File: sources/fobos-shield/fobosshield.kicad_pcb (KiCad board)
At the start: 2 copper layers, 83.8 x 63.5 mm, 156 parts, among them J1 Target, J10 ADCin, J11 PP1, J12 PP2, J13 Clock, J14 Trigger, J15 CSM5VCur, J16 Conn_01x01, J17 Barrel_Jack_Switch, J18 Conn_01x02, J19 Conn_01x02, J2 Glitch, J20 CSM3V3Cur, J21 GND, J22 GND, J3 Analog, J4 IOH, J5 SPI, J6 Analog2, J7 Power, J8 IOL, J9 SPI2, Q1 IRF7807Z, Q2 IRLML2502, Q3 BSS123, Q4 BSS84, U1 NMA0509SC, U10 INA225, U11 INA225, U12 LD1117S33TR_SOT223, U2 NMA0509SC, U3 LM317L_SO8, U4 LM337L_SO8, U5 LD59015, U6 LD3985G33R_TSOT23, U7 AD8331, U8 TPS7A7100_VQFN16, U9 AD9215

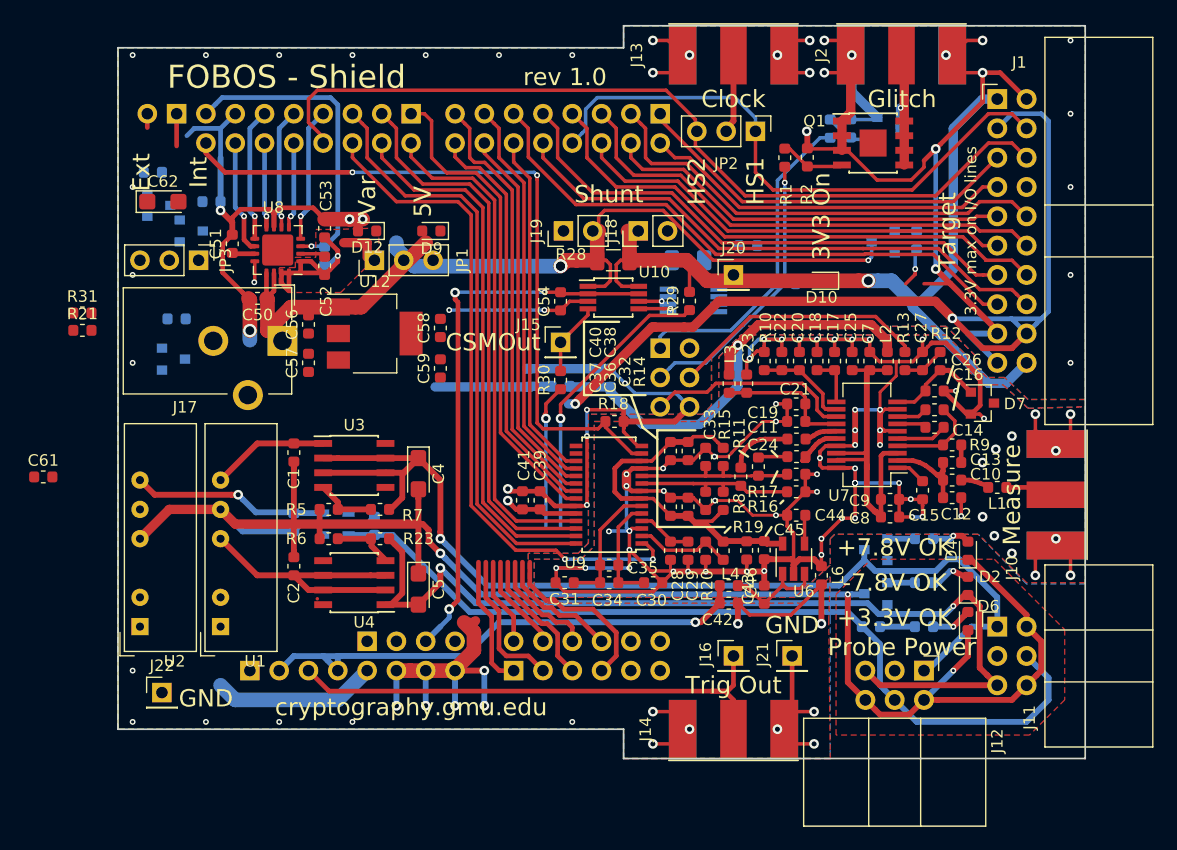
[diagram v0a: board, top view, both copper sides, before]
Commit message: variable power new layout
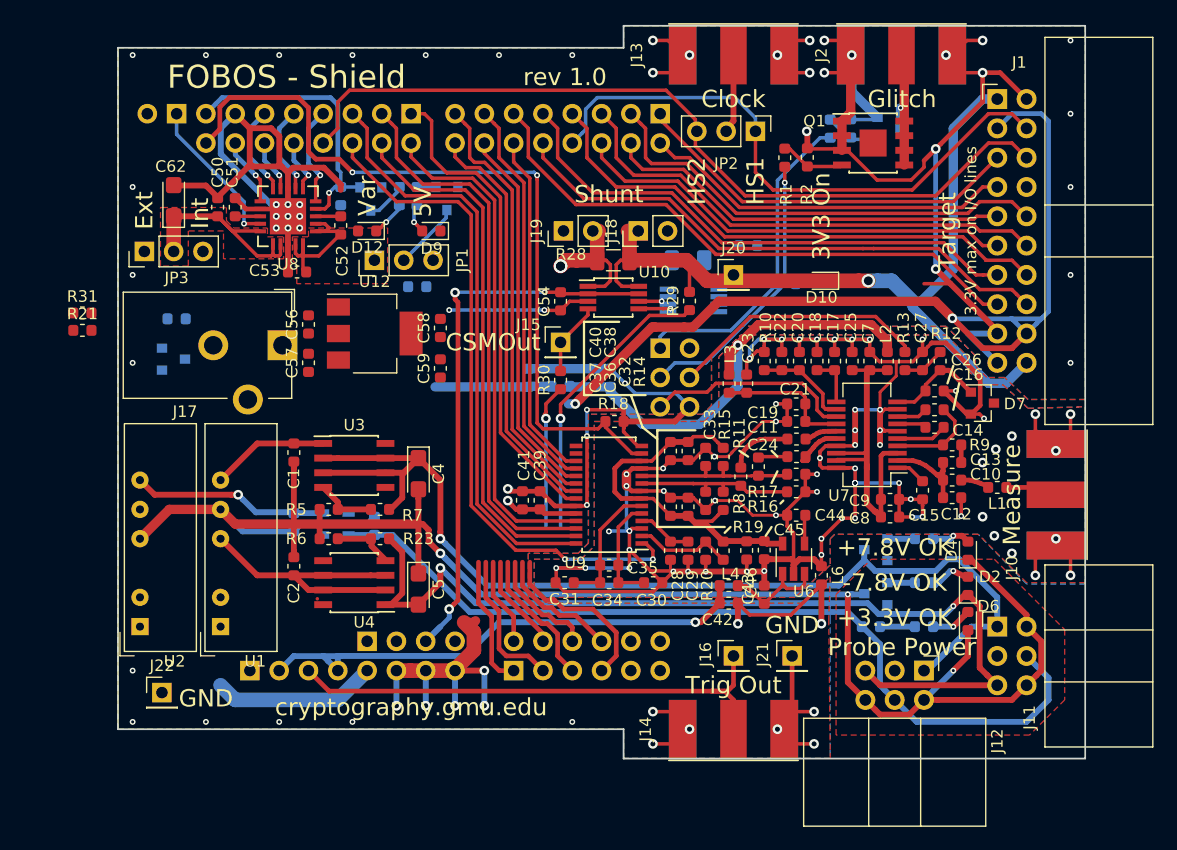
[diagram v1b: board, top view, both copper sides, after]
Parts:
- removed Q4: BSS84, Package_TO_SOT_SMD:SOT-23
- removed R34: 10K, Resistor_SMD:R_0603_1608Metric
- C61: moved to B.Cu
- U8: value TPS7A7100_VQFN16 -> TPS7A7100_VQFN20; footprint cerg:Texas_S-PVQFN-N16_EP2.7x2.7mm -> Package_DFN_QFN:Texas_VQFN-RGW-20
- moved R27 43.5 mm to (62.7, 37.6)
- moved D8 38.0 mm to (65.3, 37.8), turned to 270 degrees
- moved C61 36.4 mm to (62.8, 45.5), turned to 180 degrees
- moved Q3 18.4 mm to (58.7, 37.9), turned to 270 degrees
- moved R35 16.3 mm to (61.2, 37.6), turned to 270 degrees
- moved C50 8.62 mm to (45.5, 38.6), turned to 90 degrees
- moved R22 5.37 mm to (56.1, 37.6), turned to 90 degrees
- moved JP3 4.76 mm to (39.1, 42.4), turned to 90 degrees
- moved C53 4.47 mm to (52.3, 44.2), turned to 180 degrees
- moved C52 3.77 mm to (56.1, 40.2)
- moved C51 3.19 mm to (47.0, 38.6)
- moved U8 3.05 mm to (51.6, 39.4)
- moved C62 0.94 mm to (41.7, 38.0), turned to 90 degrees
- moved J17 0.38 mm to (51.1, 50.5)
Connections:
- C50 pad 1: VCC -> IN
- C56 pad 1: VCC -> IN
- C57 pad 1: VCC -> IN
- C60 pad 1: VCC -> IN
- C61 pad 1: VCC -> IN
- C62 pad 1: VCC -> IN
- D12 pad 1: GND -> Net-(D12-Pad1)
- D12 pad 2: Net-(D12-Pad2) -> VCC3V3
- JP1 pad 3: VCC -> IN
- JP3 pad 2: VCC -> IN
- R35 pad 1: Net-(Q4-Pad3) -> Net-(Q3-Pad3)
- R35 pad 2: Net-(D12-Pad2) -> Net-(D12-Pad1)
- U1 pad 1: VCC -> IN
- U12 pad 3: VCC -> IN
- U2 pad 1: VCC -> IN
- U8 pad 10: PWR5 -> PWR4
- U8 pad 11: Net-(C51-Pad1) -> PWR5
- U8 pad 12: PWR_EN -> GND
- U8 pad 13: VCC -> Net-(C51-Pad1)
- U8 pad 14: VCC -> PWR_EN
- U8 pad 15: Net-(C52-Pad1) -> IN
- U8 pad 16: Net-(C52-Pad1) -> IN
- U8 pad 17: (no net) -> IN
- U8 pad 2: Net-(C52-Pad2) -> Net-(C52-Pad1)
- U8 pad 3: PWR_PG -> Net-(C52-Pad2)
- U8 pad 4: PWR0 -> PWR_PG
- U8 pad 5: PWR1 -> PWR0
- U8 pad 6: PWR2 -> PWR1
- U8 pad 7: GND -> PWR2
- U8 pad 8: PWR3 -> GND
- U8 pad 9: PWR4 -> PWR3
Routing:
- net Net-(D8-Pad1): track 54.5 -> 16.7 mm, vias 3 -> 2
- net VCC5V0: track 61.5 -> 36.7 mm
- net IN: track 0.00 -> 20.2 mm
- net PWR_EN: track 4.63 -> 13.3 mm
- net GND: track 250.4 -> 258.7 mm, vias 58 -> 63
- net ADC_CLK: track 63.5 -> 69.6 mm
- net Net-(C52-Pad1): track 19.7 -> 13.9 mm, vias 1 -> 0
- net PWR5: track 9.86 -> 5.95 mm
- net PWR4: track 11.5 -> 7.85 mm
- net Net-(Q3-Pad3): track 0.00 -> 3.47 mm
- net Net-(D12-Pad1): track 0.00 -> 3.02 mm, vias 0 -> 1
- net PWR0: track 11.6 -> 8.70 mm
- net PWR1: track 7.52 -> 4.67 mm
- net PWR3: track 7.86 -> 5.03 mm
- net PWR2: track 10.9 -> 8.20 mm
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- added copper zone on F.Cu, net IN

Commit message: 3V3 CSM layouted
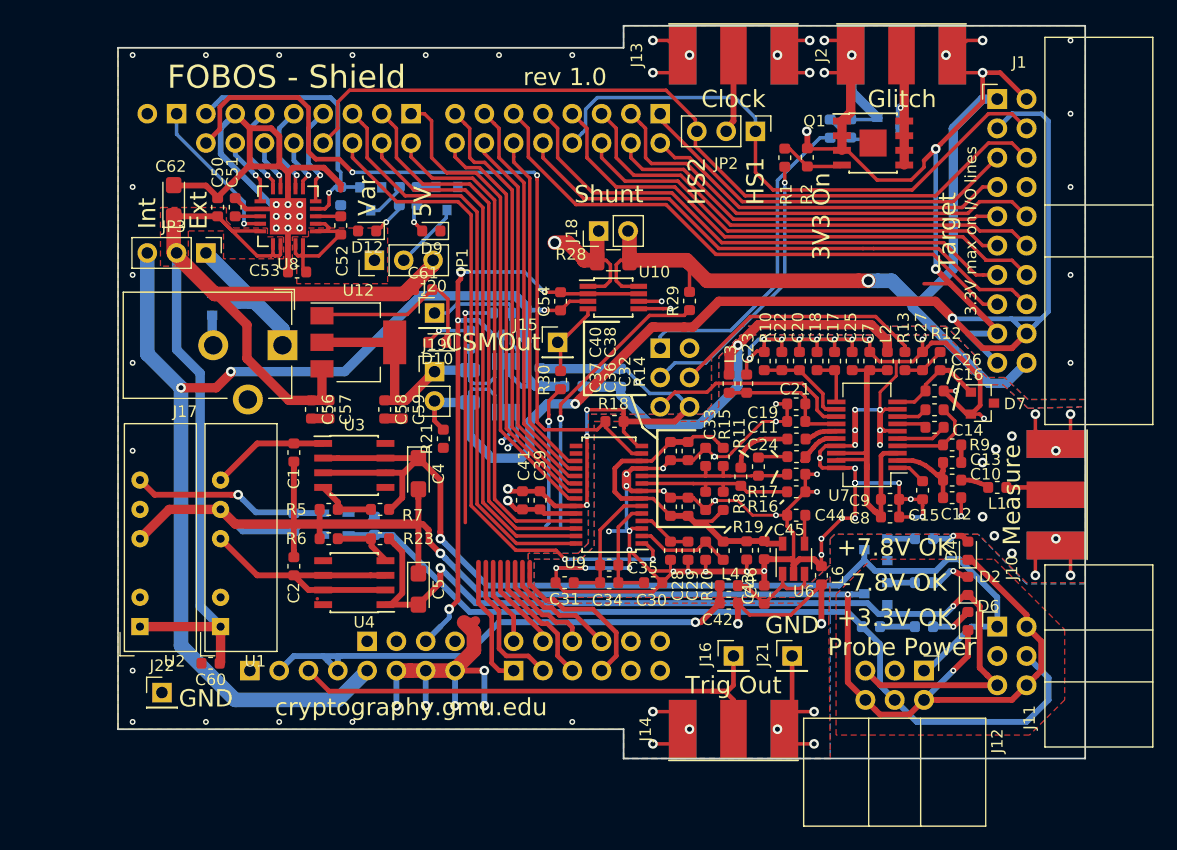
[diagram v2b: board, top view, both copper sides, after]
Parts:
- C60, C61: moved to F.Cu
- R31: moved to B.Cu
- moved R31 36.4 mm to (70.1, 47.8)
- moved D10 33.7 mm to (64.5, 50.3)
- moved R21 32.7 mm to (65.0, 58.6), turned to 90 degrees
- moved C60 30.0 mm to (44.9, 78.1), turned to 180 degrees
- moved R33 27.9 mm to (67.3, 50.1), turned to 90 degrees
- moved J20 26.1 mm to (64.3, 47.8)
- moved C55 21.9 mm to (71.0, 49.7), turned to 180 degrees
- moved R32 21.8 mm to (67.3, 54.1), turned to 270 degrees
- moved U11 17.9 mm to (70.4, 54.1), turned to 270 degrees
- moved J19 16.5 mm to (64.3, 52.8), turned to 0 degrees
- moved C58 8.55 mm to (59.9, 56.1), turned to 270 degrees
- moved C56 7.37 mm to (53.6, 56.1), turned to 270 degrees
- moved D11 6.45 mm to (46.0, 47.0)
- moved JP3 5.34 mm to (44.5, 42.5), turned to 270 degrees
- moved C59 4.85 mm to (61.5, 56.1), turned to 270 degrees
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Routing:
- net IN: track 20.2 -> 112.9 mm
- net VCC5V0: track 36.7 -> 108.3 mm, vias 2 -> 3
- net Net-(C58-Pad1): track 0.00 -> 26.3 mm
- net CSM3V3: track 79.9 -> 106.3 mm
- net GND: track 258.7 -> 279.4 mm, vias 63 -> 64
- net /Ardu/A3: track 15.0 -> 35.5 mm, vias 0 -> 1
- net XADCGND: track 47.5 -> 60.6 mm, vias 3 -> 4
- net Net-(D11-Pad1): track 0.00 -> 12.7 mm
- net CSM3V3Cur: track 0.00 -> 12.0 mm
- net Net-(D10-Pad2): track 0.00 -> 4.07 mm, vias 0 -> 1
- net CSM3V3Gain0: track 9.80 -> 13.2 mm, vias 0 -> 1
- net CSM3V3Gain1: track 10.9 -> 13.8 mm, vias 0 -> 1
- net 5Vclean: track 39.3 -> 38.2 mm
- net Net-(D8-Pad1): track 16.7 -> 17.7 mm, vias 2 -> 1

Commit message: all routed, needs DRC
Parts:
- added G***: LOGO, cerg:cerg, F.Cu at (97.0, 41.7)
- moved R29 1.65 mm to (84.7, 46.7)
- moved J15 0.76 mm to (75.7, 50.3)
- moved J19 0.13 mm to (64.1, 52.8)
- moved J20 0.13 mm to (64.1, 47.8)
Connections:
- J3 pad 2: CSM5VGain0 -> CSM3V3Gain1
- J3 pad 4: CSM5VGain1 -> CSM3V3Gain0
- J3 pad 6: CSM3V3Gain0 -> CSM5VGain1
- J3 pad 8: CSM3V3Gain1 -> CSM5VGain0
- R21 pad 1: /Ardu/A2 -> /Ardu/A0
- R29 pad 1: /Ardu/A0 -> /Ardu/A3
- R30 pad 1: /Ardu/A1 -> /Ardu/A2
- R31 pad 1: /Ardu/A3 -> /Ardu/A1
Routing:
- net GND: track 279.4 -> 473.8 mm, vias 64 -> 86
- net VCC3V3: track 51.9 -> 103.2 mm, vias 2 -> 6
- net CSM5VGain0: track 10.4 -> 38.4 mm, vias 1 -> 2
- net CSM5VGain1: track 10.4 -> 37.8 mm, vias 1 -> 2
- net /Ardu/A2: track 12.0 -> 29.3 mm, vias 0 -> 2
- net Net-(D8-Pad1): track 17.7 -> 32.1 mm
- net /Ardu/A0: track 36.6 -> 22.6 mm, vias 1 -> 2
- net /Ardu/A1: track 24.9 -> 37.5 mm
- net CSM3V3Gain0: track 13.2 -> 23.8 mm, vias 1 -> 3
- net CSM3V3Gain1: track 13.8 -> 22.8 mm, vias 1 -> 3
- net /Ardu/A3: track 35.5 -> 44.2 mm, vias 1 -> 2
- net Net-(D11-Pad1): track 12.7 -> 17.1 mm
- net Net-(C52-Pad1): track 13.9 -> 17.8 mm
- net Net-(C3-Pad1): track 17.0 -> 20.3 mm
- net /Power/GNDP: track 147.5 -> 150.2 mm
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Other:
- board text added: "3V3"
- board text added: "CSM"
- board text added: "CSM 5V/Var"
- board text added: "Out"
- board text added: "Shnt"
- board text removed: "3V3 On"
- board text removed: "CSMOut"
- board text removed: "Shunt"

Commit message: DRC passes
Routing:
- net GNDA: track 228.2 -> 230.5 mm, vias 65 -> 66
- net IN: track 112.9 -> 111.2 mm
- net 5Vclean: track 37.9 -> 36.6 mm
- net GND: track 473.8 -> 473.6 mm, vias 86 -> 89

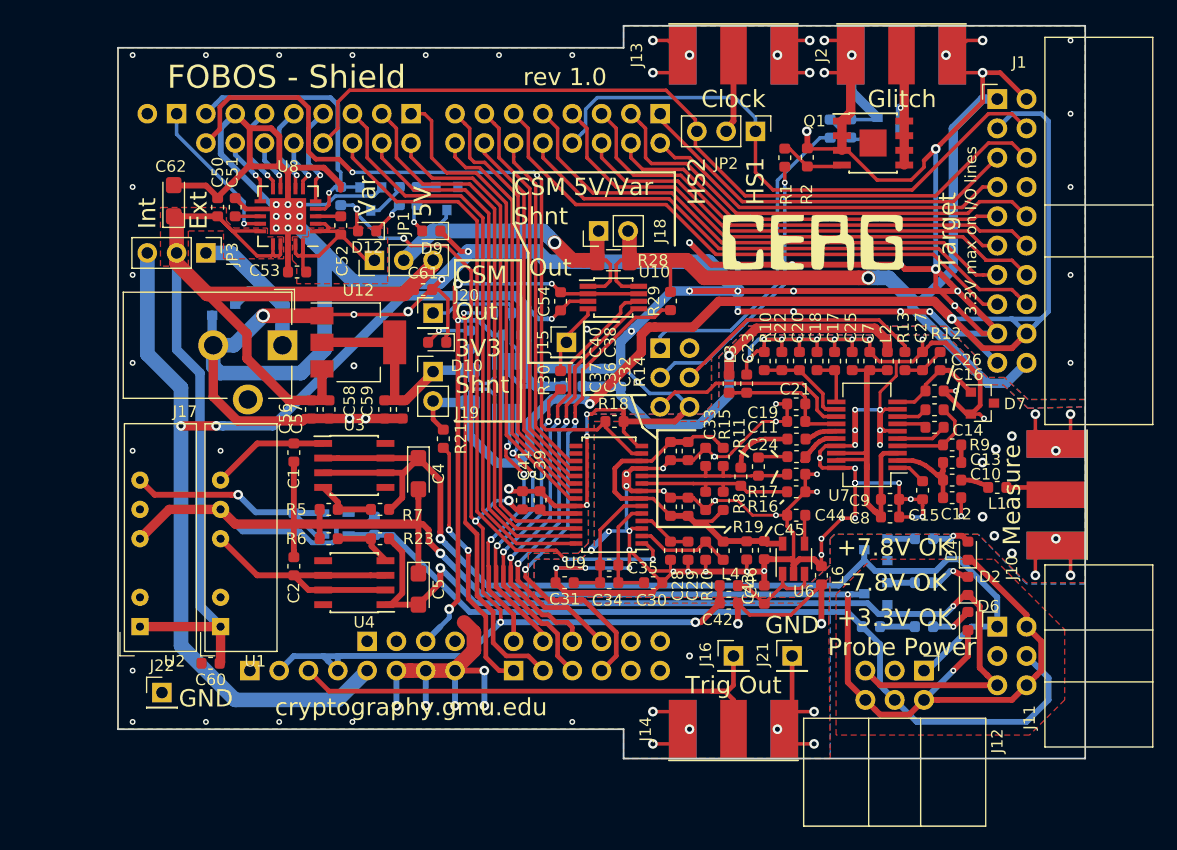
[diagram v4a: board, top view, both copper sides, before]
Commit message: made all small vias a little bit larger
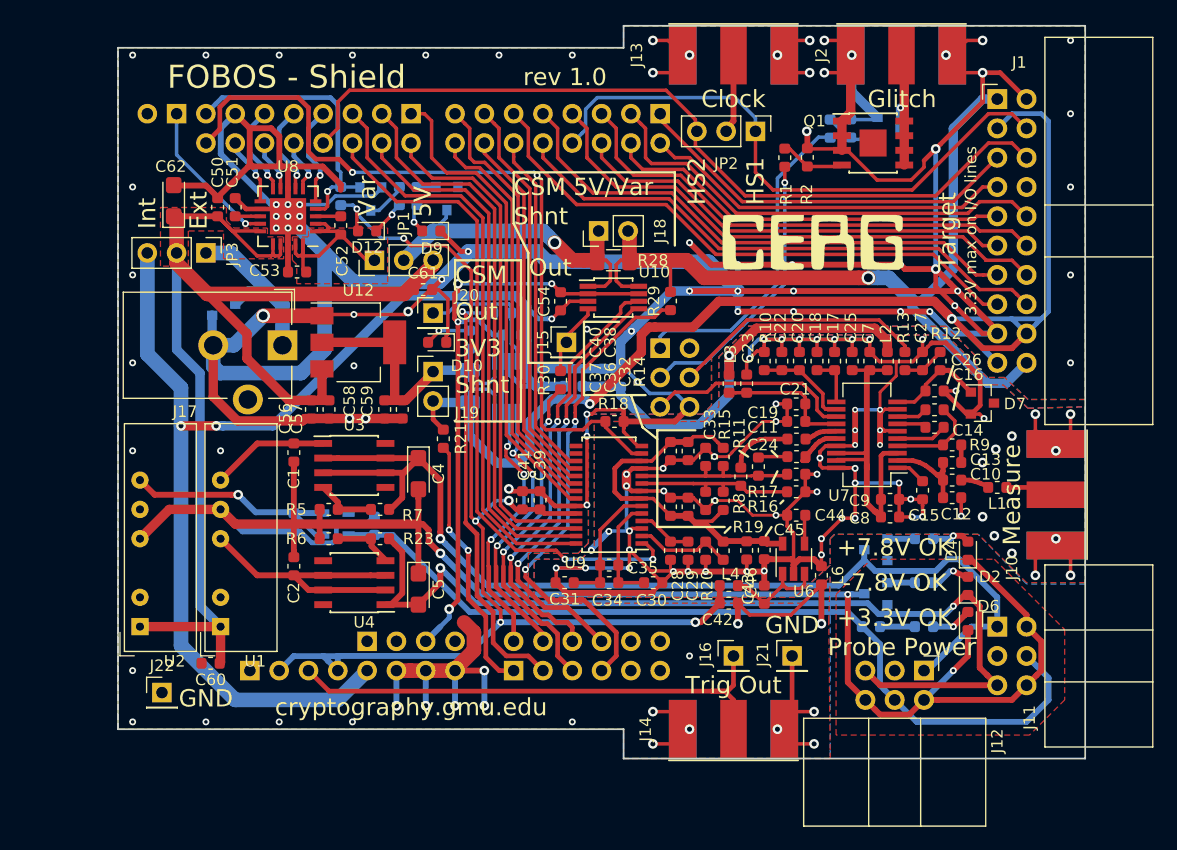
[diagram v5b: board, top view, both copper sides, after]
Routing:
- net GNDA: vias 66 -> 64

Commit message: verified probe power
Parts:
- removed G***: LOGO, cerg:cerg
- C1, C2: value 100uF -> 100nF
- C3: value 100nF -> 1uF
- D3: footprint Diode_SMD:D_0603_1608Metric -> Diode_SMD:D_SOD-323F
- U1: value NMA0509SC -> RB-0509D
- U2: value NMA0509SC -> REE-0505S
- U5: footprint Package_TO_SOT_SMD:SOT-23-5 -> cerg:sot323-5
- moved R6 7.10 mm to (62.1, 68.4), turned to 90 degrees
- moved R7 5.78 mm to (53.8, 63.8), turned to 270 degrees
- moved R23 5.56 mm to (62.1, 72.2), turned to 90 degrees
- moved C1 3.95 mm to (52.3, 63.8)
- moved C4 2.94 mm to (63.9, 64.4)
- moved U3 2.20 mm to (58.8, 62.6)
- moved C5 1.94 mm to (63.9, 70.0)
- moved R5 1.47 mm to (54.6, 66.2), turned to 0 degrees
- moved U1 0.63 mm to (46.4, 74.9)
- moved U5 0.38 mm to (55.6, 65.7), turned to 90 degrees
- moved D3 0.31 mm to (102.4, 74.9)
- moved C2 0.25 mm to (52.3, 69.7)
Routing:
- net /Power/GNDP: track 150.2 -> 181.3 mm, vias 3 -> 15
- net /Power/-7V8P: track 82.9 -> 74.3 mm
- net /Power/+7V8P: track 94.5 -> 88.7 mm
- net Net-(R5-Pad1): track 5.30 -> 3.84 mm
- net Net-(R23-Pad2): track 5.35 -> 4.33 mm
- net Net-(C1-Pad1): track 10.2 -> 11.0 mm
- net Net-(C2-Pad2): track 24.1 -> 23.4 mm
- net /Power/3V3P: track 74.8 -> 75.3 mm
- net GND: track 473.4 -> 473.6 mm, vias 89 -> 90
- added copper zone on B.Cu, net /Power/GNDP
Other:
- outline, holes or cut-outs redrawn

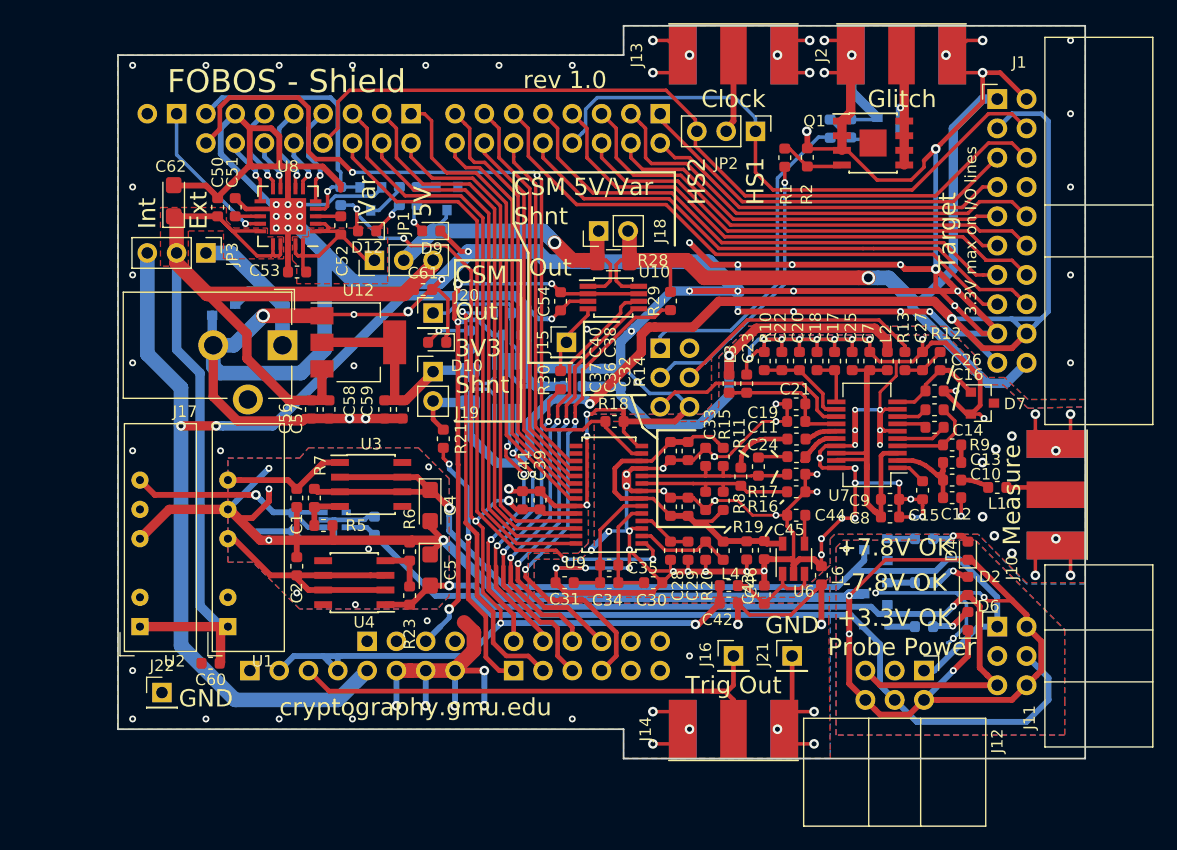
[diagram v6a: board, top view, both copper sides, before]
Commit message: power supply parts verified
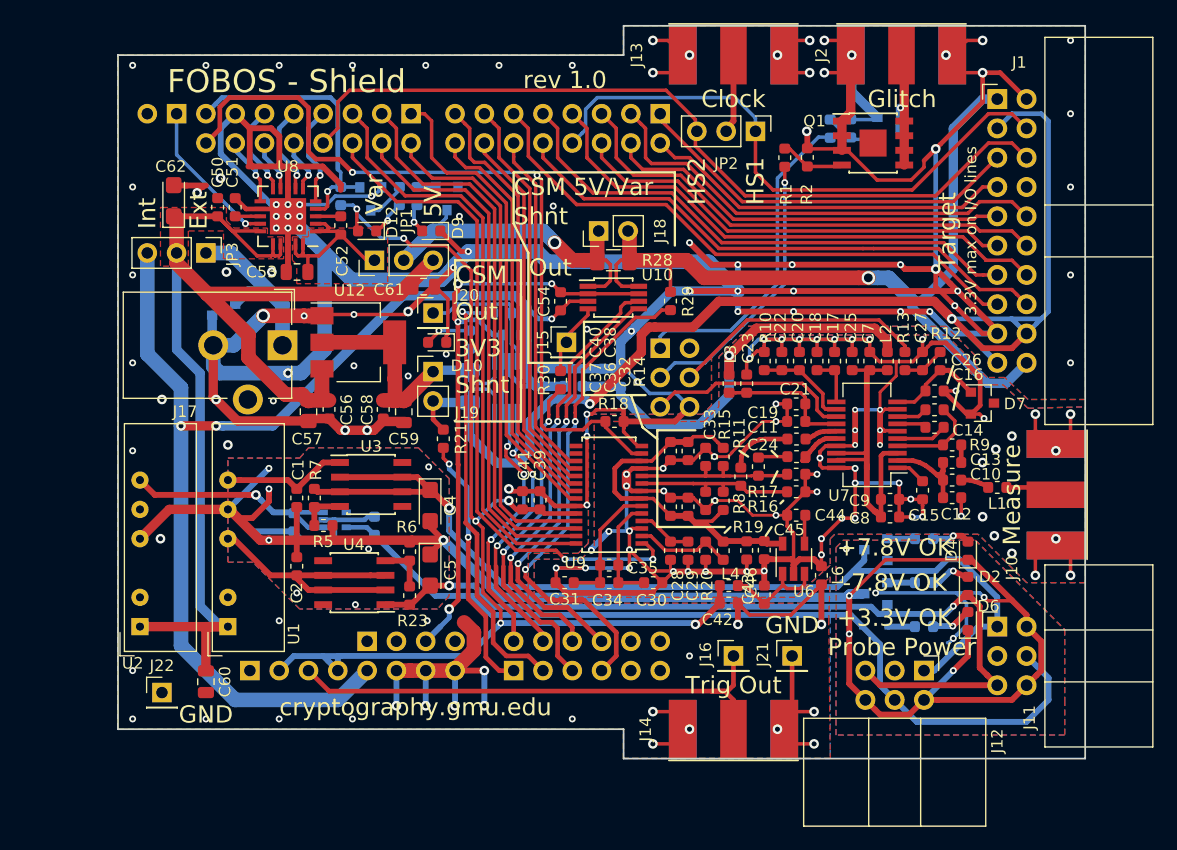
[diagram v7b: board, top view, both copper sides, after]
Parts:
- C53, C56, C59, C60, C61: footprint Capacitor_SMD:C_0603_1608Metric -> Capacitor_SMD:C_0805_2012Metric
- moved C60 1.65 mm to (44.5, 79.7), turned to 270 degrees
- moved C56 0.32 mm to (53.3, 56.3)
- moved C61 0.26 mm to (63.3, 45.5)
- moved C59 0.24 mm to (61.6, 56.3)
- moved C58 0.13 mm to (59.8, 56.1)
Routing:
- net GND: track 473.6 -> 472.3 mm, vias 90 -> 106
- net Net-(C52-Pad1): track 17.8 -> 16.7 mm
- net Net-(C58-Pad1): track 26.6 -> 27.1 mm
